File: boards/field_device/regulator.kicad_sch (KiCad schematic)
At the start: 11 parts, among them U5 HX8001-AJC

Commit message: fun
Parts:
- C12: renamed from C10; footprint Capacitor_SMD:C_0603_1608Metric -> Capacitor_SMD:C_0201_0603Metric
- C13: renamed from C11; footprint Capacitor_SMD:C_0603_1608Metric -> Capacitor_SMD:C_0201_0603Metric
- C14: renamed from C12; footprint Capacitor_SMD:C_0603_1608Metric -> Capacitor_SMD:C_0201_0603Metric
- C15: renamed from C13; footprint Capacitor_SMD:C_0603_1608Metric -> Capacitor_SMD:C_0201_0603Metric
- L1: footprint Inductor_SMD:L_0603_1608Metric -> Inductor_SMD:L_0201_0603Metric
- R12: renamed from R11; footprint Resistor_SMD:R_0603_1608Metric -> Resistor_SMD:R_0201_0603Metric
- R13: renamed from R12; footprint Resistor_SMD:R_0603_1608Metric -> Resistor_SMD:R_0201_0603Metric
- R14: renamed from R13; footprint Resistor_SMD:R_0603_1608Metric -> Resistor_SMD:R_0201_0603Metric
- R15: renamed from R14; footprint Resistor_SMD:R_0603_1608Metric -> Resistor_SMD:R_0201_0603Metric
- R16: renamed from R15; footprint Resistor_SMD:R_0603_1608Metric -> Resistor_SMD:R_0201_0603Metric
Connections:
- net GND: now also U5.2 (MS)
- no-connect marks 1 -> 0
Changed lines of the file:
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@@
 		(color 0 0 0 0)
-	)
-	(no_connect
-		(at 68.58 34.29)
 	)
 	(wire
@@
 	)
 	(symbol
+		(lib_id "power:GND")
+		(at 68.58 34.29 270)
+		(unit 1)
+		(body_style 1)
+		(exclude_from_sim no)
+		(in_bom yes)
+		(on_board yes)
+		(in_pos_files yes)
+		(dnp no)
+		(fields_autoplaced yes)
+		(property "Reference" "#PWR049"
+			(at 62.23 34.29 0)
+			(hide yes)
+			(show_name no)
+			(do_not_autoplace no)
+			(effects
+				(font
+					(size 1.27 1.27)
+				)
+			)
+		)
+		(property "Value" "GND"
+			(at 64.77 34.2899 90)
+			(show_name no)
+			(do_not_autoplace no)
+			(effects
+				(font
+					(size 1.27 1.27)
+				)
+				(justify right)
+			)
+		)
+		(property "Footprint" ""
+			(at 68.58 34.29 0)
+			(hide yes)
+			(show_name no)
+			(do_not_autoplace no)
+			(effects
+				(font
+					(size 1.27 1.27)
+				)
+			)
+		)
+		(property "Datasheet" ""
+			(at 68.58 34.29 0)
+			(hide yes)
+			(show_name no)
+			(do_not_autoplace no)
+			(effects
+				(font
+					(size 1.27 1.27)
+				)
+			)
+		)
+		(property "Description" "Power symbol creates a global label with name \"GND\" , ground"
+			(at 68.58 34.29 0)
+			(hide yes)
+			(show_name no)
+			(do_not_autoplace no)
+			(effects
+				(font
+					(size 1.27 1.27)
+				)
+			)
+		)
+		(pin "1"
+		)
+		(instances
+			(project "field_device"
+				(path "/99623870-118f-49fe-bbf0-fb0b890db442/e9c11804-cc5e-4b00-a5de-7502c32ebb51/ed5659f9-5584-4daa-a017-4d4def535a07"
+					(reference "#PWR049")
+					(unit 1)
+				)
+			)
+		)
+	)
+	(symbol
 		(lib_id "power:+3.3V")
 		(at 105.41 41.91 270)
@@
 		(dnp no)
 		(fields_autoplaced yes)
-		(property "Reference" "#PWR027"
+		(property "Reference" "#PWR032"
 			(at 101.6 41.91 0)
 			(hide yes)
@@
 			(project "field_device"
 				(path "/99623870-118f-49fe-bbf0-fb0b890db442/e9c11804-cc5e-4b00-a5de-7502c32ebb51/ed5659f9-5584-4daa-a017-4d4def535a07"
-					(reference "#PWR027")
+					(reference "#PWR032")
 					(unit 1)
 				)
@@
 		(dnp no)
 		(fields_autoplaced yes)
-		(property "Reference" "#PWR026"
+		(property "Reference" "#PWR031"
 			(at 102.87 55.88 0)
 			(hide yes)
@@
 			(project "field_device"
 				(path "/99623870-118f-49fe-bbf0-fb0b890db442/e9c11804-cc5e-4b00-a5de-7502c32ebb51/ed5659f9-5584-4daa-a017-4d4def535a07"
-					(reference "#PWR026")
+					(reference "#PWR031")
 					(unit 1)
 				)
@@
 		(dnp no)
 		(fields_autoplaced yes)
-		(property "Reference" "#PWR028"
+		(property "Reference" "#PWR033"
 			(at 118.11 29.21 0)
 			(hide yes)
@@
 			(project "field_device"
 				(path "/99623870-118f-49fe-bbf0-fb0b890db442/e9c11804-cc5e-4b00-a5de-7502c32ebb51/ed5659f9-5584-4daa-a017-4d4def535a07"
-					(reference "#PWR028")
+					(reference "#PWR033")
 					(unit 1)
 				)
@@
 			)
 		)
-		(property "Footprint" "Inductor_SMD:L_0603_1608Metric"
+		(property "Footprint" "Inductor_SMD:L_0201_0603Metric"
 			(at 55.88 36.83 0)
 			(hide yes)
@@
 		(dnp no)
 		(fields_autoplaced yes)
-		(property "Reference" "C13"
+		(property "Reference" "C15"
 			(at 106.68 44.4499 0)
 			(show_name no)
@@
 			)
 		)
-		(property "Footprint" "Capacitor_SMD:C_0603_1608Metric"
+		(property "Footprint" "Capacitor_SMD:C_0201_0603Metric"
 			(at 103.8352 49.53 0)
 			(hide yes)
@@
 			(project "field_device"
 				(path "/99623870-118f-49fe-bbf0-fb0b890db442/e9c11804-cc5e-4b00-a5de-7502c32ebb51/ed5659f9-5584-4daa-a017-4d4def535a07"
-					(reference "C13")
+					(reference "C15")
 					(unit 1)
 				)
@@
 		(dnp no)
 		(fields_autoplaced yes)
-		(property "Reference" "#PWR024"
+		(property "Reference" "#PWR029"
 			(at 59.69 17.78 0)
 			(hide yes)
@@
 			(project "field_device"
 				(path "/99623870-118f-49fe-bbf0-fb0b890db442/e9c11804-cc5e-4b00-a5de-7502c32ebb51/ed5659f9-5584-4daa-a017-4d4def535a07"
-					(reference "#PWR024")
+					(reference "#PWR029")
 					(unit 1)
 				)
@@
 		(dnp no)
 		(fields_autoplaced yes)
-		(property "Reference" "R12"
+		(property "Reference" "R13"
 			(at 62.23 26.6699 0)
 			(show_name no)
@@
 			)
 		)
-		(property "Footprint" "Resistor_SMD:R_0603_1608Metric"
+		(property "Footprint" "Resistor_SMD:R_0201_0603Metric"
 			(at 61.468 27.94 90)
 			(hide yes)
@@
 			(project "field_device"
 				(path "/99623870-118f-49fe-bbf0-fb0b890db442/e9c11804-cc5e-4b00-a5de-7502c32ebb51/ed5659f9-5584-4daa-a017-4d4def535a07"
-					(reference "R12")
+					(reference "R13")
 					(unit 1)
 				)
@@
 		(dnp no)
 		(fields_autoplaced yes)
-		(property "Reference" "R13"
+		(property "Reference" "R14"
 			(at 93.98 36.8299 0)
 			(show_name no)
@@
 			)
 		)
-		(property "Footprint" "Resistor_SMD:R_0603_1608Metric"
+		(property "Footprint" "Resistor_SMD:R_0201_0603Metric"
 			(at 89.662 38.1 90)
 			(hide yes)
@@
 			(project "field_device"
 				(path "/99623870-118f-49fe-bbf0-fb0b890db442/e9c11804-cc5e-4b00-a5de-7502c32ebb51/ed5659f9-5584-4daa-a017-4d4def535a07"
-					(reference "R13")
+					(reference "R14")
 					(unit 1)
 				)
@@
 		(dnp no)
 		(fields_autoplaced yes)
-		(property "Reference" "C11"
+		(property "Reference" "C13"
 			(at 30.48 44.4499 0)
 			(show_name no)
@@
 			)
 		)
-		(property "Footprint" "Capacitor_SMD:C_0603_1608Metric"
+		(property "Footprint" "Capacitor_SMD:C_0201_0603Metric"
 			(at 27.6352 49.53 0)
 			(hide yes)
@@
 			(project "field_device"
 				(path "/99623870-118f-49fe-bbf0-fb0b890db442/e9c11804-cc5e-4b00-a5de-7502c32ebb51/ed5659f9-5584-4daa-a017-4d4def535a07"
-					(reference "C11")
+					(reference "C13")
 					(unit 1)
 				)
@@
 		(dnp no)
 		(fields_autoplaced yes)
-		(property "Reference" "#PWR023"
+		(property "Reference" "#PWR028"
 			(at 26.67 55.88 0)
 			(hide yes)
@@
 			(project "field_device"
 				(path "/99623870-118f-49fe-bbf0-fb0b890db442/e9c11804-cc5e-4b00-a5de-7502c32ebb51/ed5659f9-5584-4daa-a017-4d4def535a07"
-					(reference "#PWR023")
+					(reference "#PWR028")
 					(unit 1)
 				)
@@
 		(dnp no)
 		(fields_autoplaced yes)
-		(property "Reference" "R14"
+		(property "Reference" "R15"
 			(at 100.33 22.86 90)
 			(show_name no)
@@
 			)
 		)
-		(property "Footprint" "Resistor_SMD:R_0603_1608Metric"
+		(property "Footprint" "Resistor_SMD:R_0201_0603Metric"
 			(at 100.33 30.988 90)
 			(hide yes)
@@
 			(project "field_device"
 				(path "/99623870-118f-49fe-bbf0-fb0b890db442/e9c11804-cc5e-4b00-a5de-7502c32ebb51/ed5659f9-5584-4daa-a017-4d4def535a07"
-					(reference "R14")
+					(reference "R15")
 					(unit 1)
 				)
@@
 		(dnp no)
 		(fields_autoplaced yes)
-		(property "Reference" "R11"
+		(property "Reference" "R12"
 			(at 21.59 35.56 90)
 			(show_name no)
@@
 			)
 		)
-		(property "Footprint" "Resistor_SMD:R_0603_1608Metric"
+		(property "Footprint" "Resistor_SMD:R_0201_0603Metric"
 			(at 21.59 43.688 90)
 			(hide yes)
@@
 			(project "field_device"
 				(path "/99623870-118f-49fe-bbf0-fb0b890db442/e9c11804-cc5e-4b00-a5de-7502c32ebb51/ed5659f9-5584-4daa-a017-4d4def535a07"
-					(reference "R11")
+					(reference "R12")
 					(unit 1)
 				)
@@
 		(dnp no)
 		(fields_autoplaced yes)
-		(property "Reference" "#PWR025"
+		(property "Reference" "#PWR030"
 			(at 62.23 41.91 0)
 			(hide yes)
@@
 			(project "field_device"
 				(path "/99623870-118f-49fe-bbf0-fb0b890db442/e9c11804-cc5e-4b00-a5de-7502c32ebb51/ed5659f9-5584-4daa-a017-4d4def535a07"
-					(reference "#PWR025")
+					(reference "#PWR030")
 					(unit 1)
 				)
@@
 		(dnp no)
 		(fields_autoplaced yes)
-		(property "Reference" "C12"
+		(property "Reference" "C14"
 			(at 92.71 21.59 90)
 			(show_name no)
@@
 			)
 		)
-		(property "Footprint" "Capacitor_SMD:C_0603_1608Metric"
+		(property "Footprint" "Capacitor_SMD:C_0201_0603Metric"
 			(at 96.52 28.2448 0)
 			(hide yes)
@@
 			(project "field_device"
 				(path "/99623870-118f-49fe-bbf0-fb0b890db442/e9c11804-cc5e-4b00-a5de-7502c32ebb51/ed5659f9-5584-4daa-a017-4d4def535a07"
-					(reference "C12")
+					(reference "C14")
 					(unit 1)
 				)
@@
 		(dnp no)
 		(fields_autoplaced yes)
-		(property "Reference" "R15"
+		(property "Reference" "R16"
 			(at 107.95 22.86 90)
 			(show_name no)
@@
 			)
 		)
-		(property "Footprint" "Resistor_SMD:R_0603_1608Metric"
+		(property "Footprint" "Resistor_SMD:R_0201_0603Metric"
 			(at 107.95 30.988 90)
 			(hide yes)
@@
 			(project "field_device"
 				(path "/99623870-118f-49fe-bbf0-fb0b890db442/e9c11804-cc5e-4b00-a5de-7502c32ebb51/ed5659f9-5584-4daa-a017-4d4def535a07"
-					(reference "R15")
+					(reference "R16")
 					(unit 1)
 				)
@@
 		(dnp no)
 		(fields_autoplaced yes)
-		(property "Reference" "#PWR022"
+		(property "Reference" "#PWR027"
 			(at 26.67 34.29 0)
 			(hide yes)
@@
 			(project "field_device"
 				(path "/99623870-118f-49fe-bbf0-fb0b890db442/e9c11804-cc5e-4b00-a5de-7502c32ebb51/ed5659f9-5584-4daa-a017-4d4def535a07"
-					(reference "#PWR022")
+					(reference "#PWR027")
 					(unit 1)
 				)
@@
 		(dnp no)
 		(fields_autoplaced yes)
-		(property "Reference" "C10"
+		(property "Reference" "C12"
 			(at 30.48 22.8599 0)
 			(show_name no)
@@
 			)
 		)
-		(property "Footprint" "Capacitor_SMD:C_0603_1608Metric"
+		(property "Footprint" "Capacitor_SMD:C_0201_0603Metric"
 			(at 27.6352 27.94 0)
 			(hide yes)
@@
 			(project "field_device"
 				(path "/99623870-118f-49fe-bbf0-fb0b890db442/e9c11804-cc5e-4b00-a5de-7502c32ebb51/ed5659f9-5584-4daa-a017-4d4def535a07"
-					(reference "C10")
-					(unit 1)
-				)
+					(reference "C12")
+					(unit 1)
+				)

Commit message: reorganized mcu
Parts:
- C12: value 10uF -> 10u
- C13: value 100nF -> 100n
- C14: value 1.5nF -> 1.5n
- C15: value 22uF -> 22u
- L1: value 10uH -> 10u
- R12: value 1MΩ -> 1M
- R13: value 60.4kΩ -> 60.4k
- R14: value 340kΩ -> 340k
- R15: value 15kΩ -> 15k
- R16: value 200kΩ -> 200k
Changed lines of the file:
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@@
 			)
 		)
-		(property "Value" "10uH"
+		(property "Value" "10u"
 			(at 55.88 34.29 90)
 			(show_name no)
@@
 			)
 		)
-		(property "Value" "22uF"
+		(property "Value" "22u"
 			(at 106.68 46.9899 0)
 			(show_name no)
@@
 			)
 		)
-		(property "Value" "60.4kΩ"
+		(property "Value" "60.4k"
 			(at 62.23 29.2099 0)
 			(show_name no)
@@
 			)
 		)
-		(property "Value" "340kΩ"
+		(property "Value" "340k"
 			(at 93.98 39.3699 0)
 			(show_name no)
@@
 			)
 		)
-		(property "Value" "100nF"
+		(property "Value" "100n"
 			(at 30.48 46.9899 0)
 			(show_name no)
@@
 			)
 		)
-		(property "Value" "15kΩ"
+		(property "Value" "15k"
 			(at 100.33 25.4 90)
 			(show_name no)
@@
 			)
 		)
-		(property "Value" "1MΩ"
+		(property "Value" "1M"
 			(at 21.59 38.1 90)
 			(show_name no)
@@
 			)
 		)
-		(property "Value" "1.5nF"
+		(property "Value" "1.5n"
 			(at 92.71 24.13 90)
 			(show_name no)
@@
 			)
 		)
-		(property "Value" "200kΩ"
+		(property "Value" "200k"
 			(at 107.95 25.4 90)
 			(show_name no)
@@
 			)
 		)
-		(property "Value" "10uF"
+		(property "Value" "10u"
 			(at 30.48 25.3999 0)
 			(show_name no)

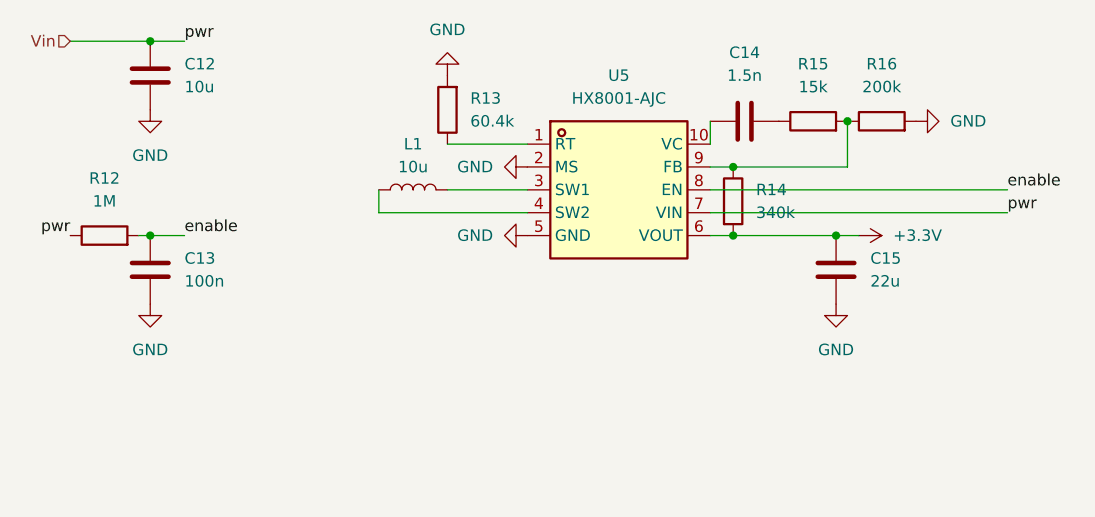
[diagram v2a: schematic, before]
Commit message: reorganized regulator
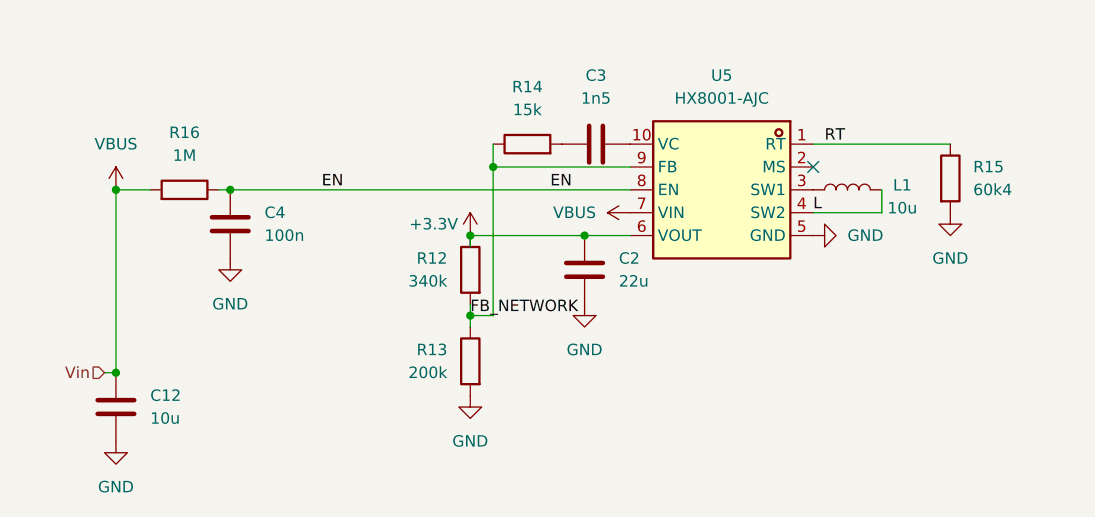
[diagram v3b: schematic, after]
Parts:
- removed C13: 100n, Capacitor_SMD:C_0201_0603Metric, symbol Device:C
- removed C14: 1.5n, Capacitor_SMD:C_0201_0603Metric, symbol Device:C
- removed C15: 22u, Capacitor_SMD:C_0201_0603Metric, symbol Device:C
- added C2: 22u, Sensor_Current:LEM_HX02-P, symbol Device:C
- added C3: 1n5, Sensor_Current:LEM_HX02-P, symbol Device:C
- added C4: 100n, Sensor_Current:LEM_HX02-P, symbol Device:C
- L1: footprint Inductor_SMD:L_0201_0603Metric -> (none)
- R12: value 1M -> 340k; footprint Resistor_SMD:R_0201_0603Metric -> (none)
- R13: value 60.4k -> 200k; footprint Resistor_SMD:R_0201_0603Metric -> (none)
- R14: value 340k -> 15k; footprint Resistor_SMD:R_0201_0603Metric -> (none)
- R15: value 15k -> 60k4; footprint Resistor_SMD:R_0201_0603Metric -> (none)
- R16: value 200k -> 1M; footprint Resistor_SMD:R_0201_0603Metric -> (none)
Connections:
- net +3.3V: now also R12.1, C2.1; no longer R14.2
- net GND: now also R15.2, C2.2, C4.2; no longer R16.2, U5.2 (MS)
- net at L1.1: now also U5.3 (SW1); no longer U5.4 (SW2)
- net L: now reaches L1.2
- net L: now also U5.4 (SW2); no longer U5.3 (SW1)
- net FB_NETWORK: now reaches R13.1
- net FB_NETWORK: now also R12.2, R14.1, U5.9 (FB); no longer U5.1 (RT)
- net at U5.10 (VC): now also C3.2
- net RT: now reaches R15.1
- net RT: now also U5.1 (RT)
- net Vin renamed VBUS
- net VBUS: now also R16.2; no longer R12.1
- net enable renamed EN
- net EN: now also R16.1, C4.1; no longer R12.2
- new net: C3.1, R14.2
- no-connect marks 0 -> 1
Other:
- moved on the sheet: C12, U5

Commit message: added satus leds
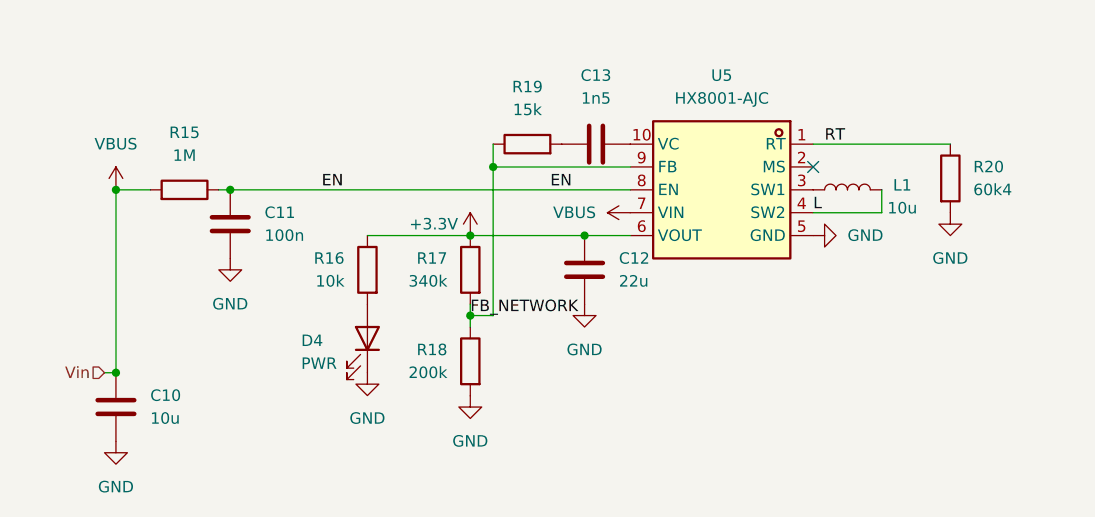
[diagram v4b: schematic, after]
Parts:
- added D4: PWR, symbol Device:LED
- added R16: 10k, symbol Device:R
- renumbered C12 to C10, C4 to C11, C2 to C12, C3 to C13, R16 to R15, R12 to R17, R13 to R18, R14 to R19, R15 to R20
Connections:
- net +3.3V: now also R16.1
- net GND: now also D4.1 (K)
- new net: D4.2 (A), R16.2
